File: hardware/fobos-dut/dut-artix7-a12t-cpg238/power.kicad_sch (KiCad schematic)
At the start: 76 parts, among them J10 Barrel_Jack_Switch, J3 575-8, J4 Glitch, J5 Conn_01x02, J6 Measure, J8 575-8, J9 Measure, Q10 BSS138, Q7 FDS9435A, Q8 MMBT3904, Q9 MMBT3904, SW2 SW_DIP_x03, U10 BGA2801, U8 LTC3569EFE#PBF, U9 INA225

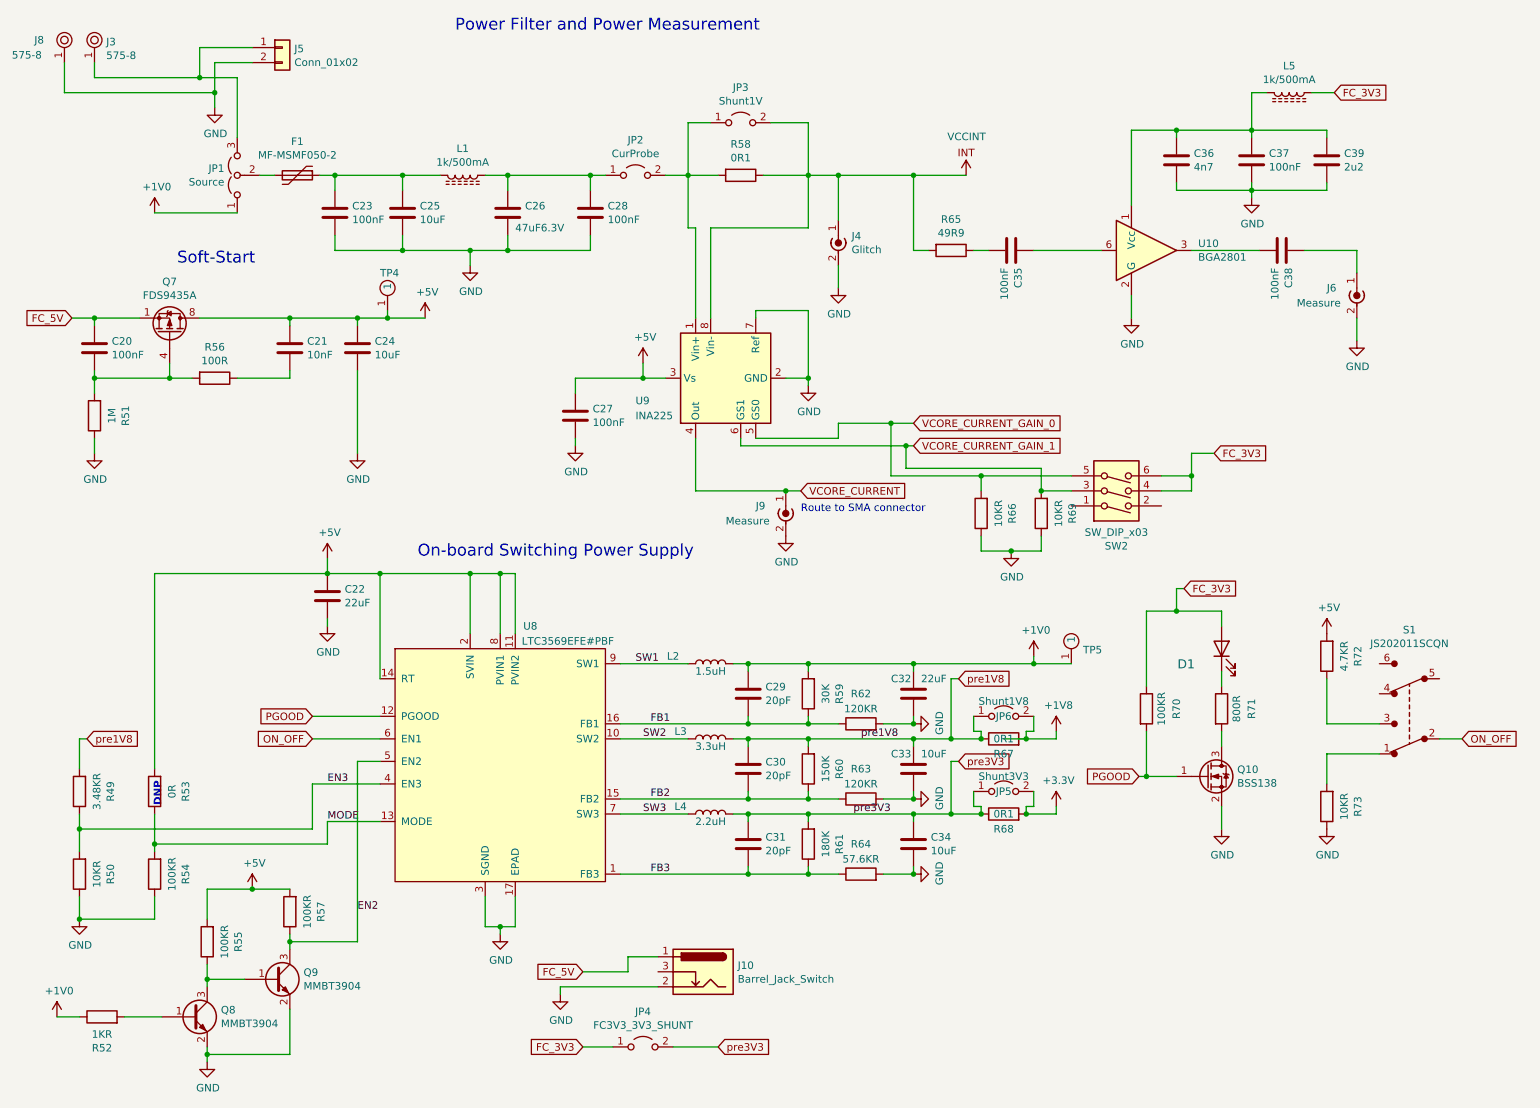
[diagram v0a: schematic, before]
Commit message: cleaned up FBDA7 rev1 added BOM, fixed bugs in schematic
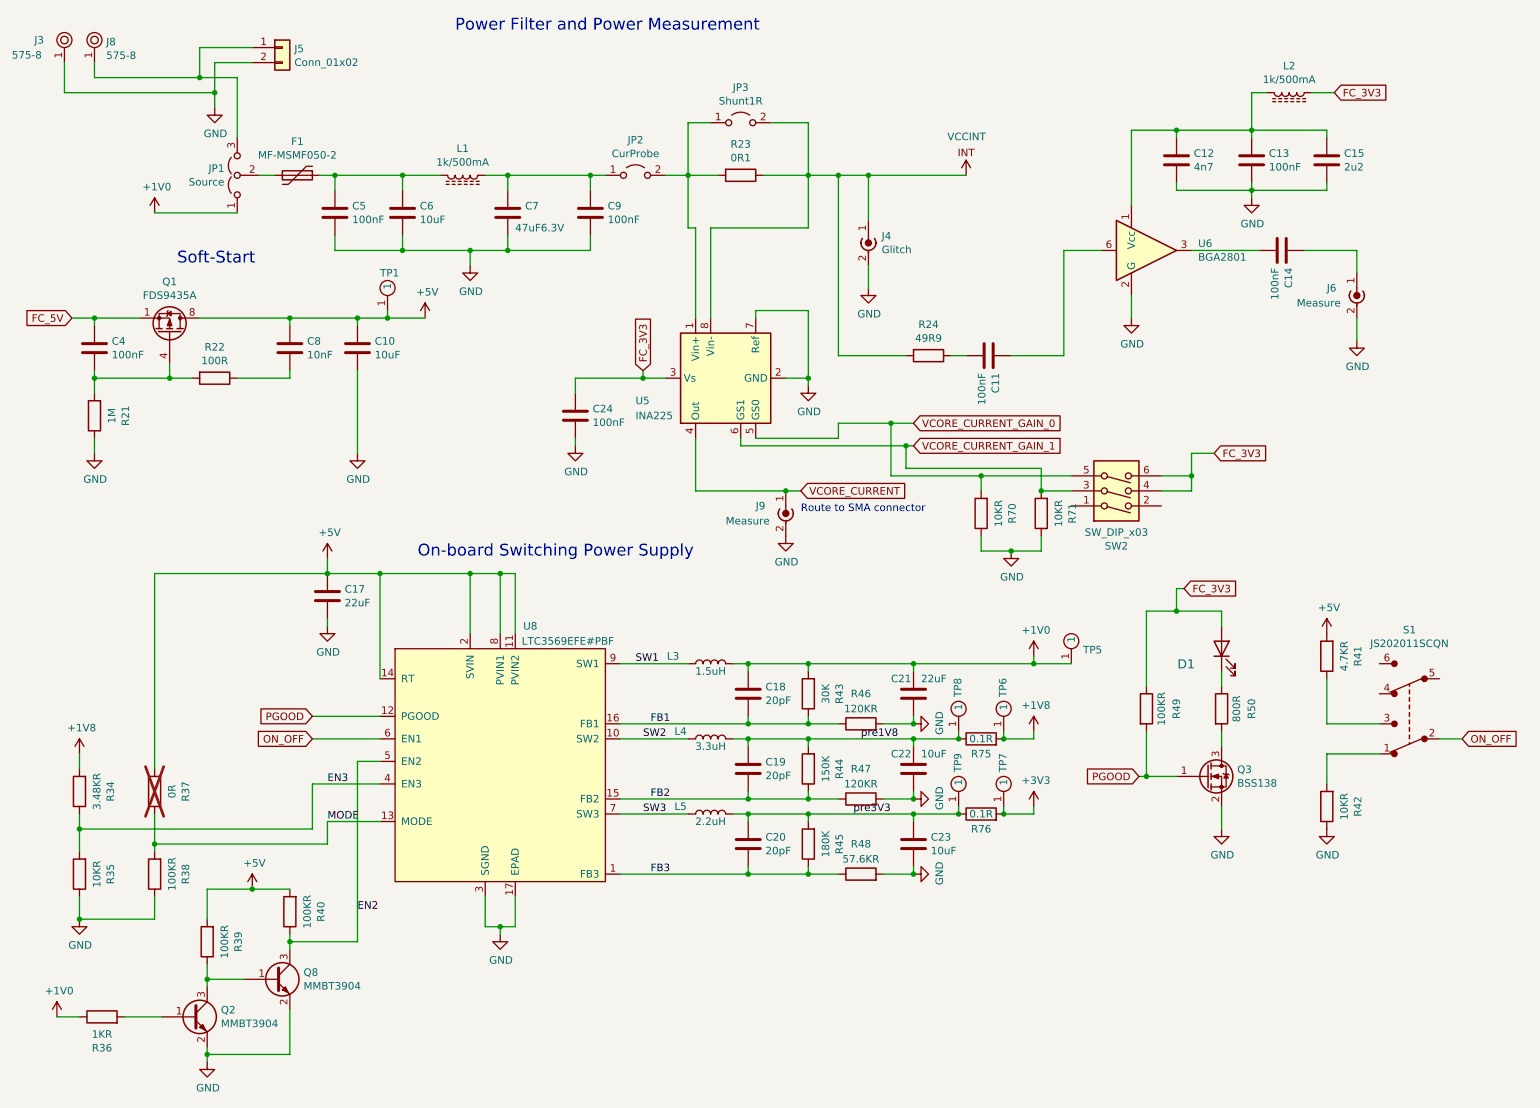
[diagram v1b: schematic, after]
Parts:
- removed J10: Barrel_Jack_Switch, cerg:BarrelJack_CUI_PJ-102AH_Horizontal, symbol Connector:Barrel_Jack_Switch
- removed JP4: FC3V3_3V3_SHUNT, Connector_PinHeader_2.54mm:PinHeader_1x02_P2.54mm_Vertical, symbol Jumper:Jumper_2_Open
- removed JP5: Shunt3V3, Connector_PinHeader_2.54mm:PinHeader_1x02_P2.54mm_Vertical, symbol Jumper:Jumper_2_Open
- removed JP6: Shunt1V8, Connector_PinHeader_2.54mm:PinHeader_1x02_P2.54mm_Vertical, symbol Jumper:Jumper_2_Open
- added TP6, TP7, TP8, TP9: 5281, cerg:5281, symbol cerg:5281
- JP3: value Shunt1V -> Shunt1R
- R37: renamed from R53; now not fitted
- R75: renamed from R67; value 0R1 -> 0.1R; footprint Resistor_SMD:R_1206_3216Metric -> Resistor_SMD:R_0805_2012Metric_Pad1.20x1.40mm_HandSolder
- R76: renamed from R68; value 0R1 -> 0.1R; footprint Resistor_SMD:R_1206_3216Metric -> Resistor_SMD:R_0805_2012Metric_Pad1.20x1.40mm_HandSolder
- renumbered C24 to C10, C35 to C11, C36 to C12, C37 to C13, C38 to C14, C39 to C15, C22 to C17, C29 to C18, C30 to C19, C31 to C20, C32 to C21, C33 to C22, C34 to C23, C27 to C24, C20 to C4, C23 to C5, C25 to C6, C26 to C7, C21 to C8, C28 to C9, J8 to J3, J3 to J8, L5 to L2, L2 to L3, L3 to L4, L4 to L5, Q7 to Q1, Q8 to Q2, Q10 to Q3, Q9 to Q8, R51 to R21, R56 to R22, R58 to R23, R65 to R24, R49 to R34, R50 to R35, R52 to R36, R54 to R38, R55 to R39, R57 to R40, R72 to R41, R73 to R42, R59 to R43, R60 to R44, R61 to R45, R62 to R46, R63 to R47, R64 to R48, R70 to R49, R71 to R50, R66 to R70, R69 to R71, TP4 to TP1, U9 to U5, U10 to U6
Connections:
- net +1V8: now also R34.2, TP6.1
- net +3V3: now also TP7.1
- net +5V: no longer C24.1, U5.3 (Vs)
- net FC_3V3: now also C24.1, U5.3 (Vs)
- net pre1V8: now also TP8.1; no longer R34.2
- net pre3V3: now also TP9.1
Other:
- note removed: "DNP"
- moved on the sheet: C11, J4, R24, R75, R76
